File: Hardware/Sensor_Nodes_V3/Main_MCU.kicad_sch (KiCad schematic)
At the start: 22 parts, among them J2 Conn_01x27_Socket, J3 Conn_01x27_Socket, U2 STM32G474RBTx, U3 MCP2542FDxMF, U4 MCP2542FDxMF

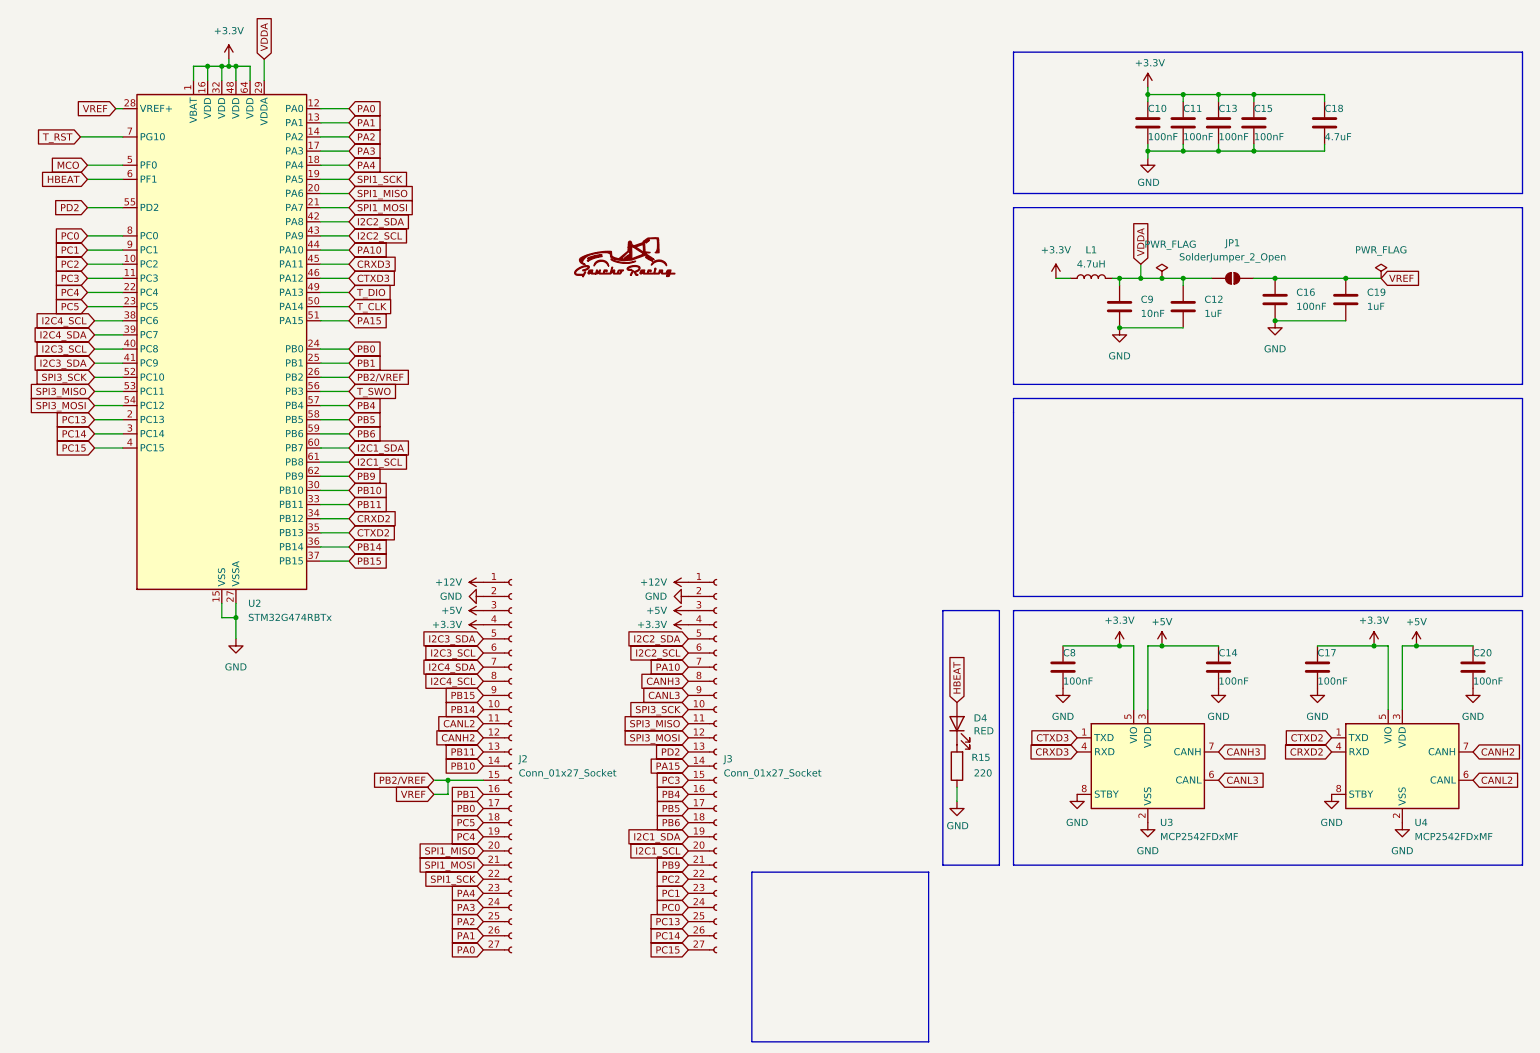
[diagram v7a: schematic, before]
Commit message: fixed pin names
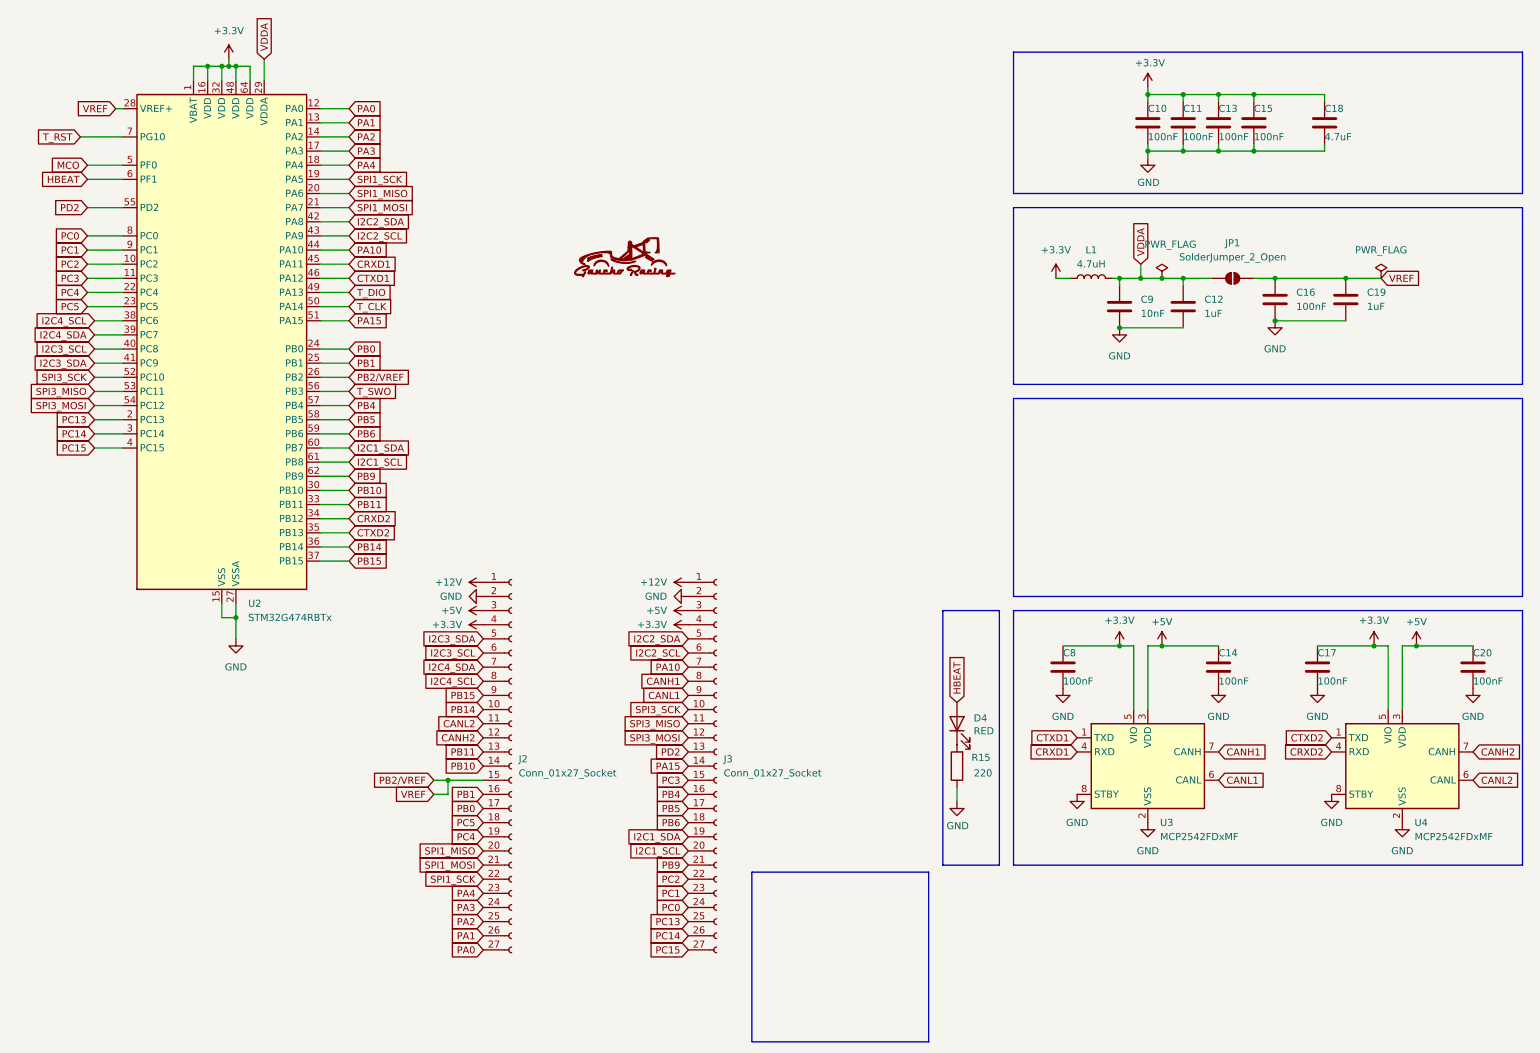
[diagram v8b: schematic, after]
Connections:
- net CANH3 renamed CANH1
- net CANL3 renamed CANL1
- net CRXD3 renamed CRXD1
- net CTXD3 renamed CTXD1
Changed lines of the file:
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@@
 		)
 	)
-	(global_label "CRXD3"
+	(global_label "CRXD1"
 		(shape input)
 		(at 71.12 57.15 0)
@@
 		)
 	)
-	(global_label "CANL3"
+	(global_label "CANL1"
 		(shape input)
 		(at 227.33 149.86 0)
@@
 		)
 	)
-	(global_label "CANH3"
+	(global_label "CANH1"
 		(shape input)
 		(at 132.08 132.08 180)
@@
 		)
 	)
-	(global_label "CTXD3"
+	(global_label "CTXD1"
 		(shape input)
 		(at 71.12 59.69 0)
@@
 		)
 	)
-	(global_label "CANL3"
+	(global_label "CANL1"
 		(shape input)
 		(at 132.08 134.62 180)
@@
 		)
 	)
-	(global_label "CTXD3"
+	(global_label "CTXD1"
 		(shape input)
 		(at 201.93 142.24 180)
@@
 		)
 	)
-	(global_label "CANH3"
+	(global_label "CANH1"
 		(shape input)
 		(at 227.33 144.78 0)
@@
 		)
 	)
-	(global_label "CRXD3"
+	(global_label "CRXD1"
 		(shape input)
 		(at 201.93 144.78 180)
